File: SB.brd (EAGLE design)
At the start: 100 x 60 mm, 59 parts, among them IC1 ATMEGA32U4NT-TQFP, IC2 MCP2515, IC3 MCP2551, J1 USB-B-PTH, X1 INPUT, X2 OUTPUT

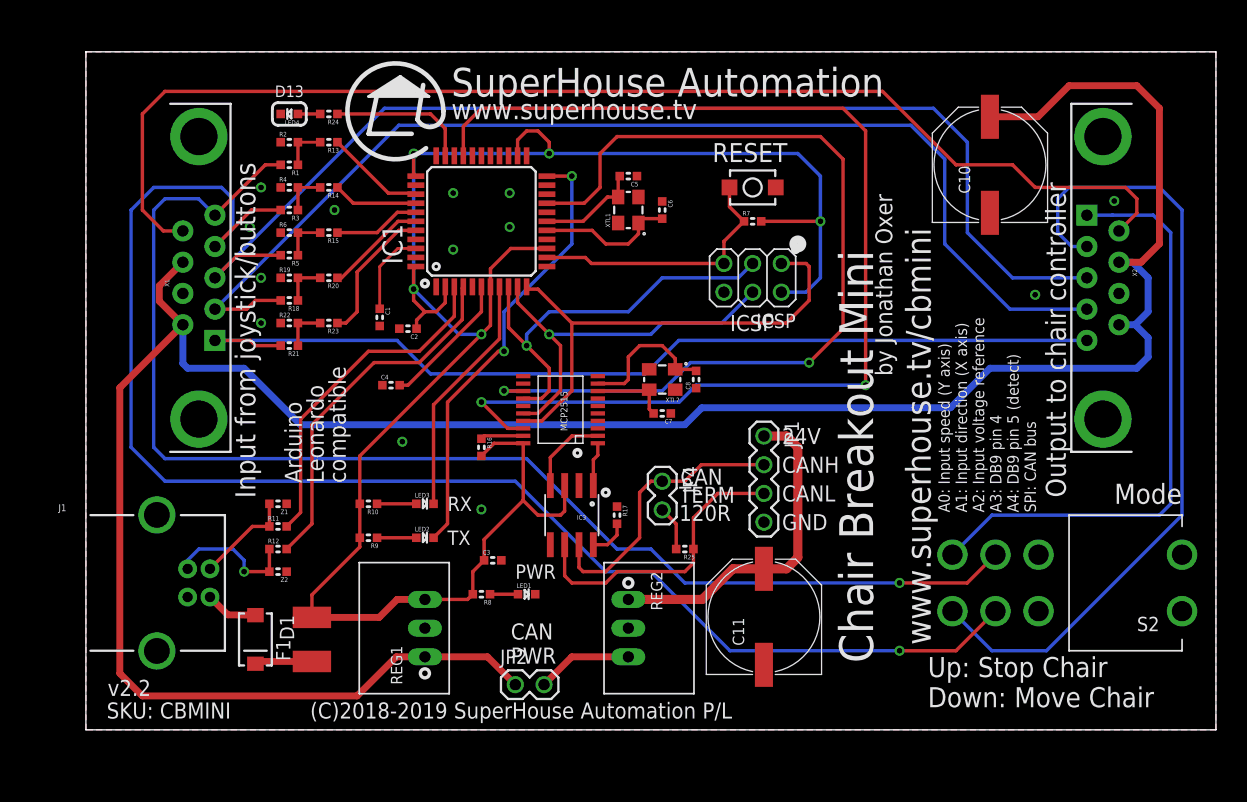
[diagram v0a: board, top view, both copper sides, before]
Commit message: Basic schematic done and rough board outline
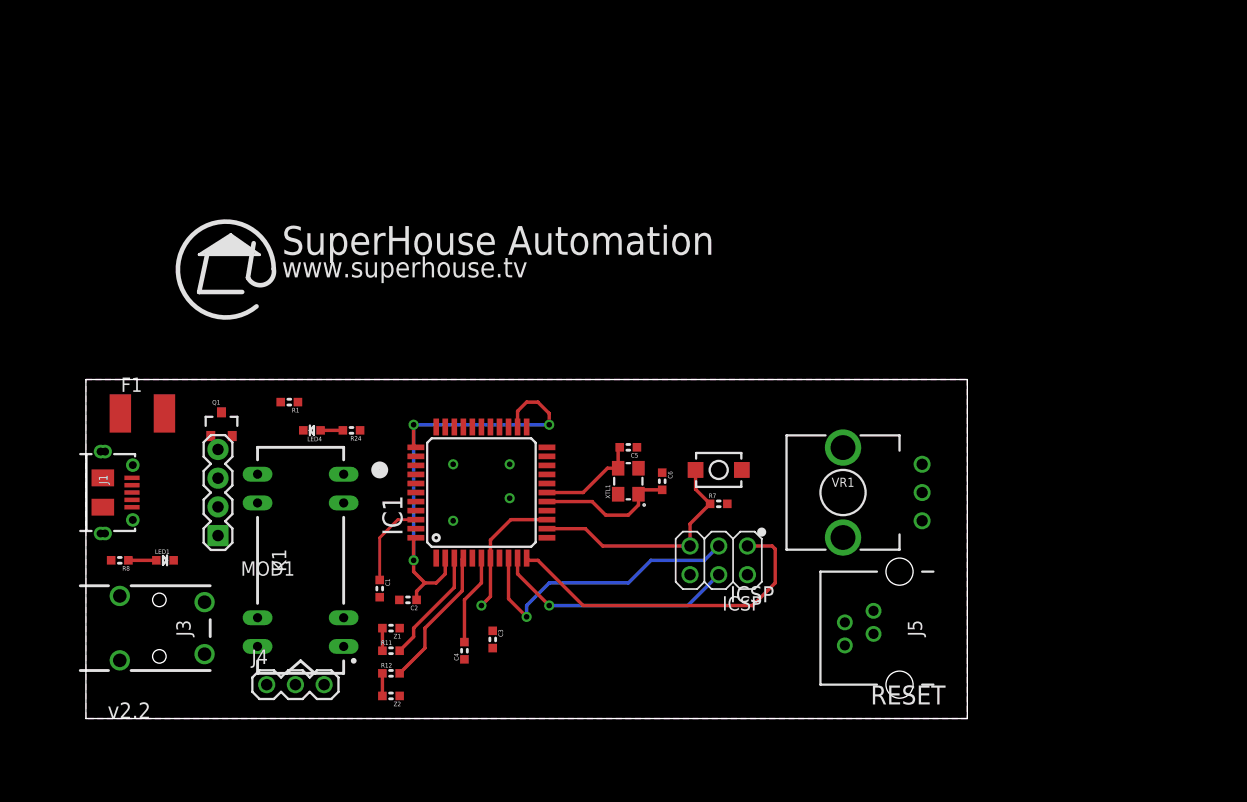
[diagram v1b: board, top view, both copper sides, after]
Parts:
- removed C10, C11: 220uF 50V, SuperHouse-DiscreteSemi:PANASONIC_G
- removed C7, C8: 15pF, SuperHouse-DiscreteSemi:C0603
- removed D1: 1N4004, SuperHouse-DiscreteSemi:SMA-DIODE
- removed IC2: MCP2515, SuperHouse-ICs:TSSOP20
- removed IC3: MCP2551, SuperHouse-ICs:SO08
- removed JP1: CAN, SuperHouse-Connectors:1X04-P
- removed JP2: PWR, SuperHouse-Connectors:1X02-P
- removed JP4: CAN TERM, SuperHouse-Connectors:1X02-P
- removed LED2: RED, SuperHouse-LEDs:LED-0603
- removed LED3: GREEN, SuperHouse-LEDs:LED-0603
- removed R10, R13, R14, R15, R20, R23, R9: 1K, SuperHouse-DiscreteSemi:R0603
- removed R16, R17: 10K, SuperHouse-DiscreteSemi:R0603
- removed R18, R19, R2, R21, R22, R3, R4, R5, R6: 47K 1%, SuperHouse-DiscreteSemi:R0603
- removed R25: 120R, SuperHouse-DiscreteSemi:R0603
- removed REG1: K7805-500R3, SuperHouse-Regulators:K78XX-500R3
- removed REG2: K7812-500R3, SuperHouse-Regulators:K78XX-500R3
- removed S2: SWITCH-DPDT3, freetronics-jon:7201SD9AV2BE
- removed X1: INPUT, SparkFun-Connectors:DB9_MALE
- removed X2: OUTPUT, SparkFun-Connectors:DB9
- removed XTL2: 16MHz, SuperHouse-Oscillators:CRYSTAL-SMD-3X2
- added J3: AUDIO-JACK-PJ321, SuperHouse-Connectors:AUDIO-JACK-PJ321
- added J4: (no value), SuperHouse-Connectors:1X03-P
- added J5: RJ10-WURTH, SuperHouse-Connectors:RJ10
- added K1: HE721C-DIP, SuperHouse-Relays:HE721
- added MOD1: OLED-I2C128X32-0.91, SuperHouse-Displays:OLED-128X32-0.91
- added Q1: 2N7002, SuperHouse-DiscreteSemi:SOT23-3
- added VR1: 10k, SuperHouse-DiscreteSemi:PTV09
- J1: value USB-B-PTH -> USB-6P-SMT; device SuperHouse-Connectors:USB-B-PTH -> SuperHouse-Connectors:USB-MICROB-MB05PMXX
- R1: value 47K 1% -> 10K
- moved LED1 32.1 mm to (7.00, 15.0)
- moved R8 32.1 mm to (3.00, 15.0)
- moved LED4 28.1 mm to (20.0, 26.5)
- moved R24 28.1 mm to (23.5, 26.5)
- moved ICSP 25.2 mm to (56.0, 15.0)
- moved R7 25.2 mm to (56.0, 20.0)
- moved S1 25.2 mm to (56.0, 23.0)
- moved F1 25.0 mm to (5.00, 28.0), turned to 0 degrees
- moved C4 24.4 mm to (33.5, 7.00), turned to 90 degrees
- moved C1 24.0 mm to (26.0, 12.5)
- moved C2 24.0 mm to (28.5, 11.5)
- moved C5 24.0 mm to (48.0, 25.0)
- moved C6 24.0 mm to (51.0, 22.0)
- moved IC1 24.0 mm to (35.0, 21.0)
- moved XTL1 24.0 mm to (48.0, 22.0)
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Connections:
- removed net 12V: JP2.2, REG2.3
- removed net 24V: C11.+, JP1.1, REG2.1
- removed net CANH: IC3.7, JP1.2, JP4.1
- removed net CANL: IC3.6, JP1.3, R25.1
- removed net DETECT: R21.2, X1.5, X2.5
- removed net DIRECTION_IN: R3.2, S2.5, X1.2
- removed net DIRECTION_OUT: S2.4, X2.2
- removed net N$10: IC2.19, R16.1
- removed net N$13: IC2.2, IC3.4
- removed net N$14: C8.2, IC2.9, XTL2.1
- removed net N$16: IC3.8, R17.2
- removed net N$17: D1.C, F1.1
- removed net N$18: C7.2, IC2.8, XTL2.3
- removed net N$19: R18.1, R19.2, R20.2
- removed net N$20: JP4.2, R25.2
- removed net N$21: R21.1, R22.2, R23.2
- removed net N$8: LED3.A, R10.1
- removed net PIN4: R18.2, X1.4, X2.4
- removed net PIN6: X1.6, X2.6
- removed net REFERENCE: R5.2, X1.3, X2.3
- removed net SPEED_IN: R1.2, S2.2, X1.1
- removed net SPEED_OUT: S2.3, X2.1
- removed net VREF: C10.+, JP2.1, REG1.1, X1.7, X1.9, X2.7, X2.9
- new net CELL_DT: J5.P$3
- new net CELL_SCK: J5.P$2
- new net N$6: J4.1, K1.14
- new net RELAY: Q1.1, R1.2
- net 5V: now also J5.P$1, K1.2, MOD1.VCC, VR1.P$1; no longer IC2.20, IC3.3, R10.2, R16.2, R9.2, REG1.3
- net A0: no longer R13.1
- net A1: no longer R14.1
- net A2: no longer R15.1
- net A3: no longer R20.1
- net A4: no longer R23.1
- net D10_A11: no longer IC2.18
- net D2_SDA: now also MOD1.SDA; no longer IC2.13
- net D3_SCL: now also MOD1.SCL
- net GND: now also J1.FIX1, J1.FIX2, J1.TAB1, J1.TAB2, J5.P$4, MOD1.GND, Q1.2, R1.1, VR1.P$3; no longer C10.-, C11.-, C7.1, C8.1, IC2.10, IC3.2, J1.SHLD1, J1.SHLD2, JP1.4, R17.1, R19.1, R2.1, R22.1, R4.1, R6.1, REG1.2, REG2.2, X1.8, X2.8, XTL2.2, XTL2.4
- net MISO: no longer IC2.17
- net MOSI: no longer IC2.16
- net N$2: now also VR1.P$2; no longer R1.1, R13.2, R2.2
- net N$3: now also K1.6, Q1.3; no longer R14.2, R3.1, R4.2
- net N$4: now also J4.3, K1.1; no longer R15.2, R5.1, R6.2
- net N$7: now also J3.2, J3.4A, J3.4B, K1.7, K1.8; no longer LED2.A, R9.1
- net N$9: now also J3.3, J4.2; no longer IC2.1, IC3.1
- net RXLED_SS: no longer LED3.C
- net SCK: no longer IC2.14
- net TX_LED: no longer LED2.C
- net USB+: now also F1.1; no longer D1.A
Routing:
- net VREF: track 218.0 -> 0.00 mm
- net DIRECTION_IN: track 128.7 -> 0.00 mm, vias 1 -> 0
- net 5V: track 176.8 -> 53.7 mm, vias 5 -> 4
- net SPEED_IN: track 115.6 -> 0.00 mm, vias 1 -> 0
- net PIN6: track 109.1 -> 0.00 mm
- net D10_A11: track 101.5 -> 0.00 mm, vias 2 -> 0
- net PIN4: track 101.2 -> 0.00 mm
- net REFERENCE: track 100.9 -> 0.00 mm
- net DETECT: track 85.6 -> 0.00 mm
- net D2_SDA: track 80.2 -> 0.00 mm, vias 2 -> 0
- net DIRECTION_OUT: track 72.1 -> 0.00 mm
- net SPEED_OUT: track 53.2 -> 0.00 mm
- net TX_LED: track 39.6 -> 0.00 mm, vias 2 -> 0
- net 24V: track 29.7 -> 0.00 mm
- net CANL: track 26.3 -> 0.00 mm
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- added copper zone on layer 16, net 5V
- removed copper zone on layer 16, net GND
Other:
- board size 100 x 60 mm -> 78 x 30 mm
- board text removed: "120R"
- board text removed: "24V"
- board text removed: "A0: Input speed (Y axis) A1: Input direction (X axis) A2: Input voltage reference A3: DB9 pin 4 A4: DB9 pin 5 (detect) SPI: CAN bus"
- board text removed: "CAN"
- board text removed: "CAN PWR"
- board text removed: "CANH"
- board text removed: "CANL"
- board text removed: "Chair Breakout Mini"
- board text removed: "D13"
- board text removed: "GND"
- board text removed: "Input from joystick/buttons"
- board text removed: "Mode"
- board text removed: "Output to chair controller"
- board text removed: "PWR"
- board text removed: "RX"
- board text removed: "TERM"
- board text removed: "TX"
- board text removed: "Up: Stop Chair Down: Move Chair"
- board text removed: "by Jonathan Oxer"

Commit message: Replaced pot with rotary encoder, switched input and output sides
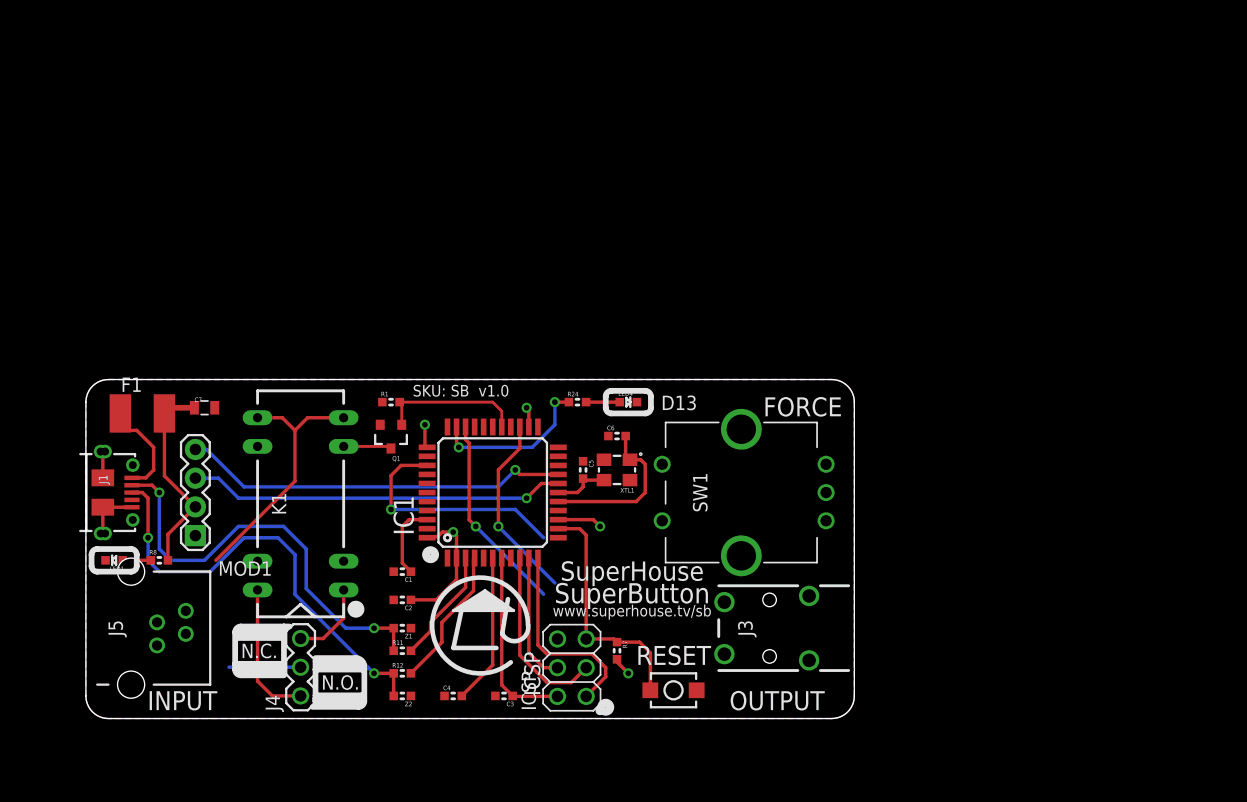
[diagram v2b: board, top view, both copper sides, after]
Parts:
- removed VR1: 10k, SuperHouse-DiscreteSemi:PTV09
- added C7: 10uF, SuperHouse-DiscreteSemi:C0805
- added SW1: ENCODER, SuperHouse-Switches:PEC12R
- J4: value (none) -> NO/NC
- moved J5 68.0 mm to (4.00, 9.00), turned to 270 degrees
- moved J3 61.0 mm to (64.0, 9.00), turned to 90 degrees
- moved LED4 28.1 mm to (48.0, 29.0), turned to 0 degrees
- moved R24 20.2 mm to (43.5, 29.0), turned to 0 degrees
- moved S1 19.9 mm to (52.0, 3.50)
- moved ICSP 16.1 mm to (43.0, 5.50), turned to 90 degrees
- moved R7 15.8 mm to (47.0, 7.00), turned to 270 degrees
- moved Q1 15.0 mm to (27.0, 26.0), turned to 180 degrees
- moved R1 9.00 mm to (27.0, 29.0), turned to 0 degrees
- moved C6 5.66 mm to (47.0, 26.0), turned to 0 degrees
- moved C3 5.10 mm to (37.0, 3.00), turned to 180 degrees
- moved K1 5.00 mm to (19.0, 20.0)
- moved LED1 4.50 mm to (2.50, 15.0), turned to 180 degrees
- moved C5 4.47 mm to (44.0, 23.0), turned to 270 degrees
- moved C4 4.12 mm to (32.5, 3.00), turned to 0 degrees
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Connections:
- removed net CELL_DT: J5.P$3
- removed net CELL_SCK: J5.P$2
- removed net N$2: VR1.P$2
- removed net RELAY: Q1.1, R1.2
- net 5V: now also C7.1; no longer VR1.P$1
- net D4_A6: now also J5.P$3
- net D5: now also J5.P$2
- net D6_A8: now also Q1.1, R1.2
- net GND: now also C7.2; no longer VR1.P$3
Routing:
- net D+: track 2.00 -> 39.5 mm, vias 0 -> 2
- net D-: track 2.00 -> 37.9 mm, vias 0 -> 2
- net D2_SDA: track 0.00 -> 34.3 mm, vias 0 -> 1
- net D3_SCL: track 0.00 -> 33.4 mm, vias 0 -> 1
- net N$7: track 0.00 -> 22.9 mm
- net A0: track 0.13 -> 21.2 mm, vias 0 -> 1
- net D5: track 0.00 -> 17.7 mm, vias 0 -> 1
- net D4_A6: track 0.00 -> 16.7 mm, vias 0 -> 1
- net D13: track 0.00 -> 14.4 mm, vias 0 -> 2
- net D6_A8: track 0.00 -> 12.8 mm
- net N$6: track 0.00 -> 12.4 mm
- net MISO: track 30.1 -> 17.8 mm
- net SCK: track 26.0 -> 16.0 mm, vias 1 -> 0
- net MOSI: track 21.5 -> 11.5 mm, vias 1 -> 0
- net USB+: track 0.00 -> 9.36 mm
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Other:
- board size 78 x 30 mm -> 68 x 30 mm
- board text added: "(C)2019 SuperHouse Automation P/L"
- board text added: "D13"
- board text added: "FORCE"
- board text added: "INPUT"
- board text added: "N.C."
- board text added: "N.O."
- board text added: "OUTPUT"
- board text added: "SKU: SB v1.0"
- board text added: "SuperButton"
- board text added: "SuperHouse"
- board text added: "www.superhouse.tv/sb"
- board text removed: "(C)2018-2019 SuperHouse Automation P/L"
- board text removed: "SKU: CBMINI"
- board text removed: "SuperHouse Automation"
- board text removed: "v2.2"
- board text removed: "www.superhouse.tv"
- board text removed: "www.superhouse.tv/cbmini"

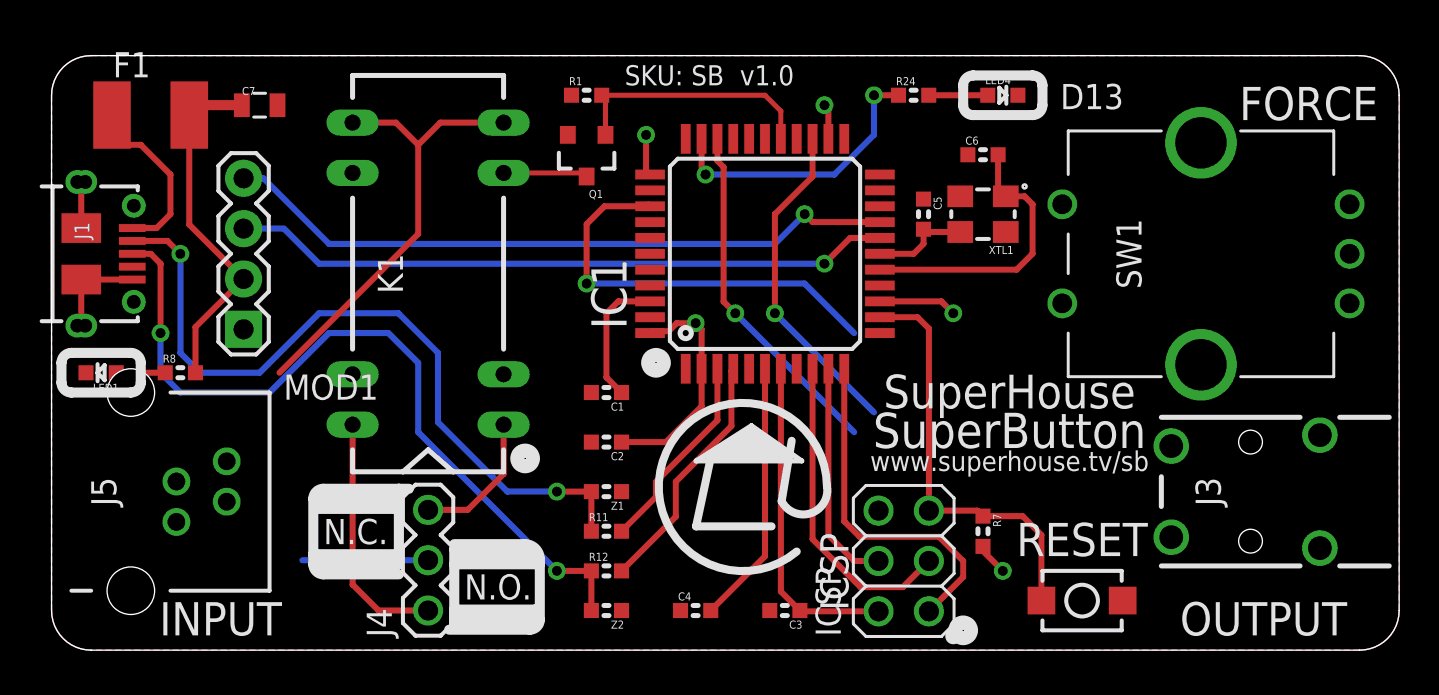
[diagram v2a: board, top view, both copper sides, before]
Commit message: Big cleanup of routing and silkscreen, with updated 3D model for OLED
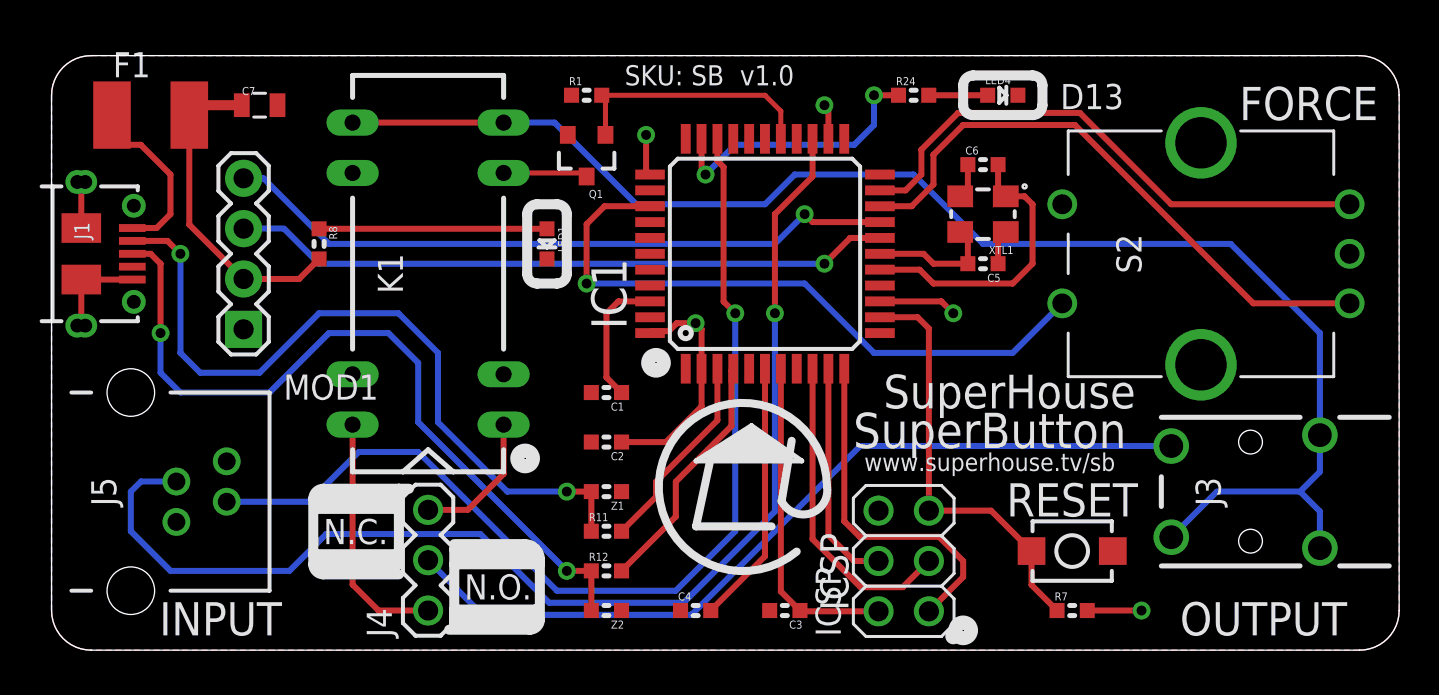
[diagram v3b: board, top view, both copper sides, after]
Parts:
- MOD1: value OLED-I2C128X32-0.91 -> OLED-I2C128X32-0.91-HEADER; device SuperHouse-Displays:OLED-128X32-0.91 -> SuperHouse-Displays:OLED-128X32-0.91-HEADER
- S2: value ENCODER -> Trigger Level
- moved LED1 23.4 mm to (25.0, 21.5), turned to 270 degrees
- moved R8 9.55 mm to (13.5, 21.5), turned to 270 degrees
- moved R7 6.02 mm to (51.5, 3.00), turned to 0 degrees
- moved C5 3.91 mm to (47.0, 20.5), turned to 180 degrees
- moved S1 2.55 mm to (51.5, 6.00)
- moved C6 0.50 mm to (47.0, 25.5)
- renumbered SW1 to S2
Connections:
- net A0: now also S2.SW1
- net D0: now also S2.A
- net D1: now also S2.B
- net GND: now also S2.C, S2.GND@1, S2.GND@2, S2.SW2
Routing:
- net N$7: track 22.9 -> 73.6 mm
- net D4_A6: track 16.7 -> 61.5 mm
- net N$9: track 6.34 -> 42.2 mm
- net D5: track 17.7 -> 51.0 mm
- net D0: track 0.00 -> 30.0 mm
- net D1: track 0.00 -> 28.0 mm
- net A0: track 21.2 -> 33.2 mm
- net N$5: track 2.48 -> 11.5 mm
- net GND: track 7.39 -> 10.9 mm
- net N$11: track 5.29 -> 6.41 mm
